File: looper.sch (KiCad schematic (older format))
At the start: 0 parts

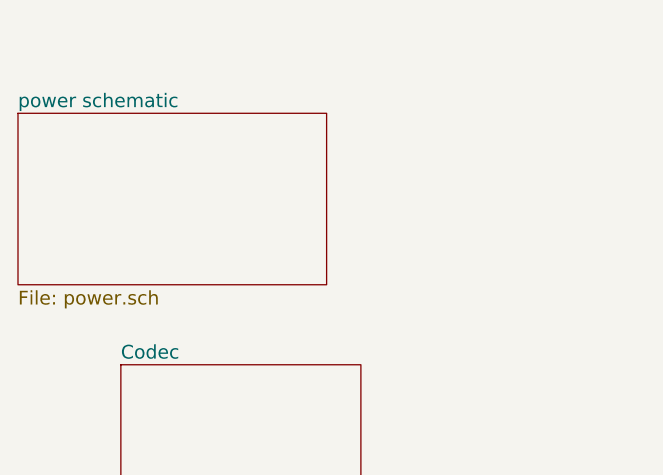
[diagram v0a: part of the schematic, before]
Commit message: ksch: add stuff that isn't on soldered prototype yet
this hopefully completes the rev. A schematics
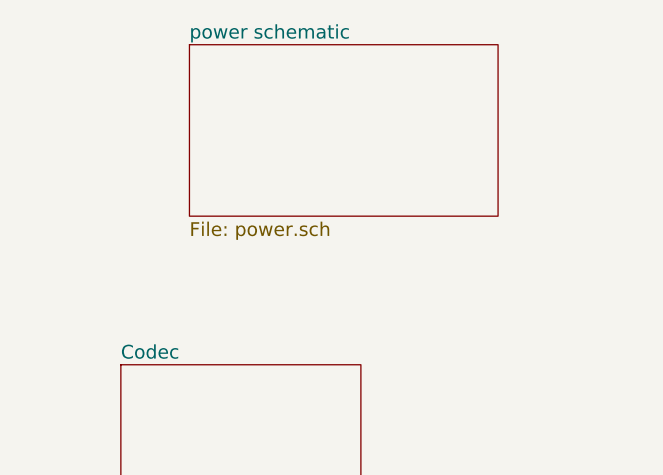
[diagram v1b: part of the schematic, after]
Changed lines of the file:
@@
-EESchema Schematic File Version 2
+EESchema Schematic File Version 3
 LIBS:openloop
 LIBS:74xgxx
@@
 LIBS:intel
 LIBS:interface
-LIBS:intersil
 LIBS:ir
 LIBS:Lattice
@@
 LIBS:zetex
 LIBS:Zilog
-EELAYER 25 0
+LIBS:looper-cache
+EELAYER 26 0
 EELAYER END
 $Descr A4 11693 8268
 encoding utf-8
 Sheet 1 4
-Title "FG_27"
-Date ""
-Rev "3.87"
-Comp "Jonathan Halmen"
+Title "OpenLoop"
+Date "2017-09-25"
+Rev "A"
+Comp ""
 Comment1 ""
 Comment2 ""
@@
 $EndDescr
 $Sheet
-S 2150 1850 1350 750
+S 2900 1550 1350 750
 U 58B3513F
 F0 "power schematic" 60
